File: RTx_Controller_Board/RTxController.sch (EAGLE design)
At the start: 204 parts, among them IC1 LTC4263, IC2 TLK110", SW1 COM08720, U1 STM32F407ZXT, U2 TPD4S012, X4 MINI-USB-32005-301

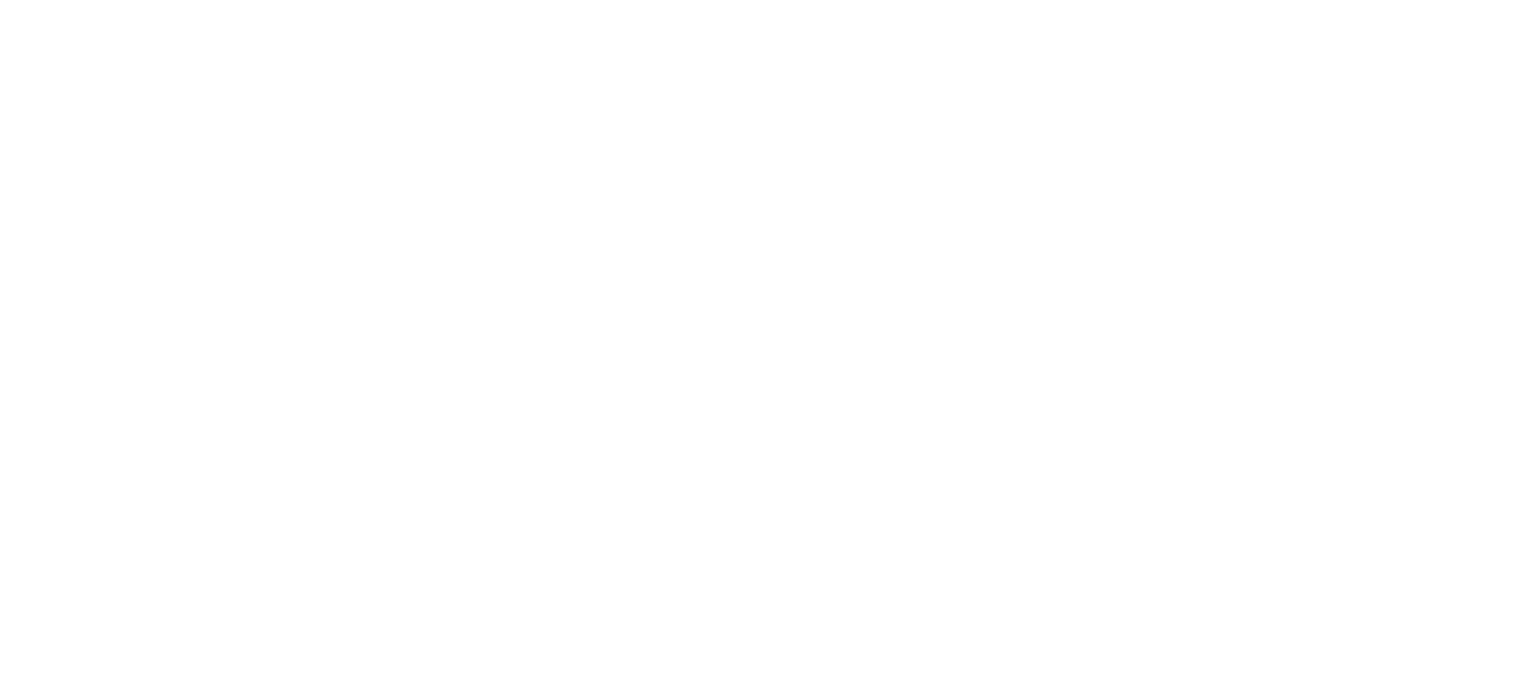
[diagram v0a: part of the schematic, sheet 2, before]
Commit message: Added PoE power supply to controller board.
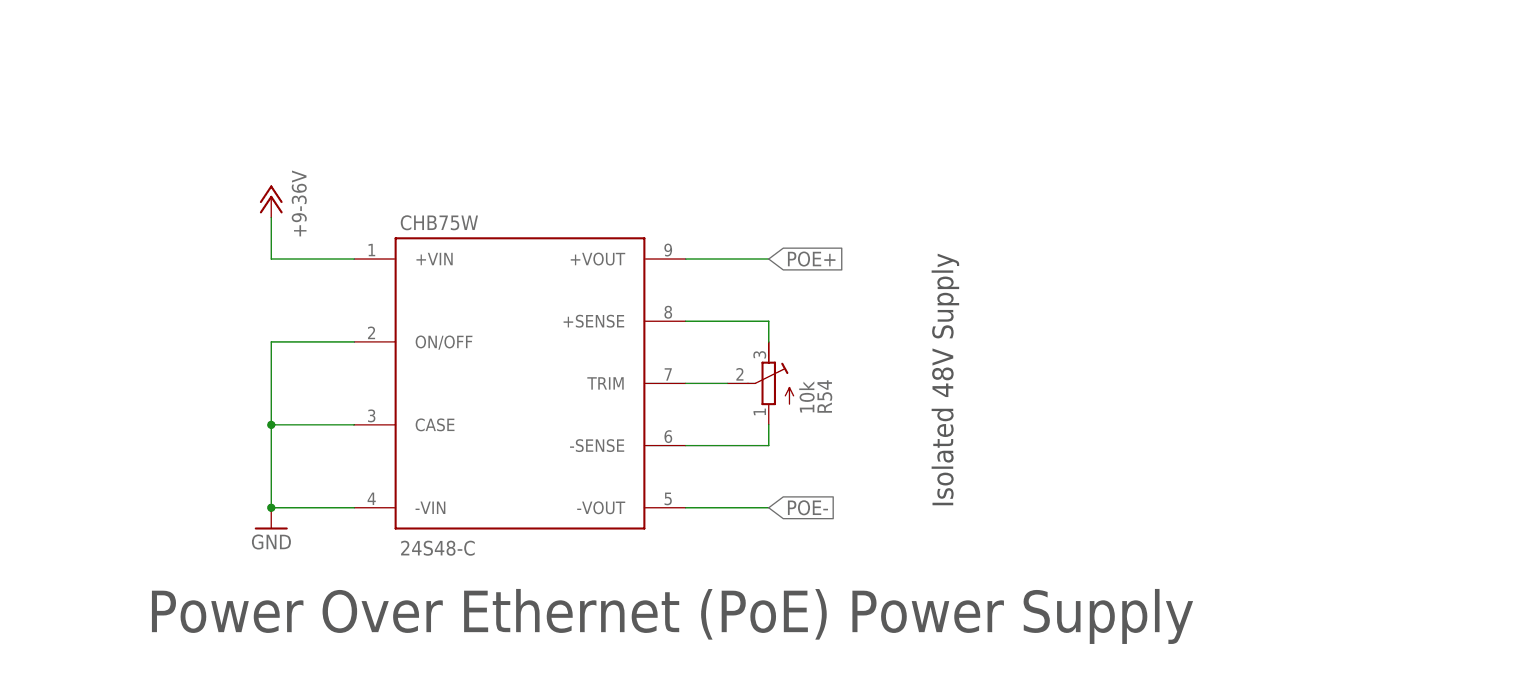
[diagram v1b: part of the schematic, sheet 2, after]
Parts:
- added 24S48-C: CHB75W, motorFeedback:CHB75W
- added R54: 10k, rcl:R-TRIMM4G/J
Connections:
- removed net DC+: C43.1, D1.C, D2.C, F1.1, IC1.VDD48, LED1.A
- removed net DC-: C43.2, C49.2, IC1.LEGACY, IC1.MIDSPAN, IC1.OSC, IC1.PWRMGT, IC1.VSS, IC1.VSS@1
- new net N$65: 24S48-C.TRIM@7, R54.S
- new net N$66: 24S48-C.-SENSE@6, R54.A
- new net N$67: 24S48-C.+SENSE@8, R54.E
- new net POE+: 24S48-C.+VOUT@9, C43.1, D1.C, D2.C, F1.1, IC1.VDD48, LED1.A
- new net POE-: 24S48-C.-VOUT@5, C43.2, C49.2, IC1.LEGACY, IC1.MIDSPAN, IC1.OSC, IC1.PWRMGT, IC1.VSS, IC1.VSS@1
- net +9-36V: now also 24S48-C.+VIN@1
- net GND: now also 24S48-C.-VIN@4, 24S48-C.CASE@3, 24S48-C.ON/OFF@2
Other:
- note added: "Power Over Ethernet (PoE) Power Supply"
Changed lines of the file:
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@@
 <part name="R52" library="motorFeedback" deviceset="R-US_" device="R0603"/>
 <part name="R53" library="motorFeedback" deviceset="R-US_" device="R0603"/>
+<part name="24S48-C" library="motorFeedback" deviceset="CHB75W" device=""/>
+<part name="R54" library="rcl" deviceset="R-TRIMM" device="4G/J" value="10k"/>
+<part name="GND97" library="motorFeedback" deviceset="GND" device=""/>
+<part name="U$7" library="motorFeedback" deviceset="+9-36V" device=""/>
 </parts>
 <sheets>
@@
 <text x="208.28" y="132.08" size="5.08" layer="97">Main Switching Power Supply</text>
 <text x="48.26" y="50.8" size="5.08" layer="97">Analog Reference Voltage Regulator</text>
+<text x="208.28" y="48.26" size="5.08" layer="97">Power Over Ethernet (PoE) Power Supply</text>
+<text x="307.086" y="63.5" size="2.54" layer="97" rot="R90">Isolated 48V Supply</text>
 </plain>
 <instances>
@@
 <instance part="REF2" gate="G$1" x="91.44" y="83.82"/>
 <instance part="P+24" gate="1" x="55.88" y="104.14"/>
+<instance part="24S48-C" gate="G$1" x="254" y="78.74" rot="MR180"/>
+<instance part="R54" gate="G$1" x="284.48" y="78.74" rot="MR0"/>
+<instance part="GND97" gate="1" x="223.52" y="60.96" rot="MR0"/>
+<instance part="U$7" gate="G$1" x="223.52" y="101.6" rot="MR0"/>
 </instances>
 <busses>
@@
 <pinref part="C24" gate="G$1" pin="2"/>
 <pinref part="GND24" gate="1" pin="GND"/>
+</segment>
+<segment>
+<pinref part="24S48-C" gate="G$1" pin="-VIN@4"/>
+<wire x1="233.68" y1="63.5" x2="223.52" y2="63.5" width="0.1524" layer="91"/>
+<pinref part="GND97" gate="1" pin="GND"/>
+<pinref part="24S48-C" gate="G$1" pin="CASE@3"/>
+<wire x1="233.68" y1="73.66" x2="223.52" y2="73.66" width="0.1524" layer="91"/>
+<wire x1="223.52" y1="73.66" x2="223.52" y2="63.5" width="0.1524" layer="91"/>
+<junction x="223.52" y="63.5"/>
+<pinref part="24S48-C" gate="G$1" pin="ON/OFF@2"/>
+<wire x1="233.68" y1="83.82" x2="223.52" y2="83.82" width="0.1524" layer="91"/>
+<wire x1="223.52" y1="83.82" x2="223.52" y2="73.66" width="0.1524" layer="91"/>
+<junction x="223.52" y="73.66"/>
 </segment>
 </net>
@@
 <pinref part="C34" gate="G$1" pin="+"/>
 </segment>
+<segment>
+<pinref part="24S48-C" gate="G$1" pin="+VIN@1"/>
+<wire x1="233.68" y1="93.98" x2="223.52" y2="93.98" width="0.1524" layer="91"/>
+<pinref part="U$7" gate="G$1" pin="+9-36V"/>
+<wire x1="223.52" y1="99.06" x2="223.52" y2="93.98" width="0.1524" layer="91"/>
+</segment>
 </net>
 <net name="+12V" class="0">
@@
 <pinref part="REF2" gate="G$1" pin="VIN@2"/>
 <pinref part="P+24" gate="1" pin="+18V"/>
+</segment>
+</net>
+<net name="N$65" class="0">
+<segment>
+<pinref part="R54" gate="G$1" pin="S"/>
+<pinref part="24S48-C" gate="G$1" pin="TRIM@7"/>
+<wire x1="279.4" y1="78.74" x2="274.32" y2="78.74" width="0.1524" layer="91"/>
+</segment>
+</net>
+<net name="N$66" class="0">
+<segment>
+<pinref part="R54" gate="G$1" pin="A"/>
+<pinref part="24S48-C" gate="G$1" pin="-SENSE@6"/>
+<wire x1="284.48" y1="73.66" x2="284.48" y2="71.12" width="0.1524" layer="91"/>
+<wire x1="284.48" y1="71.12" x2="274.32" y2="71.12" width="0.1524" layer="91"/>
+</segment>
+</net>
+<net name="N$67" class="0">
+<segment>
+<pinref part="R54" gate="G$1" pin="E"/>
+<pinref part="24S48-C" gate="G$1" pin="+SENSE@8"/>
+<wire x1="284.48" y1="83.82" x2="284.48" y2="86.36" width="0.1524" layer="91"/>
+<wire x1="284.48" y1="86.36" x2="274.32" y2="86.36" width="0.1524" layer="91"/>
+</segment>
+</net>
+<net name="POE-" class="0">
+<segment>
+<pinref part="24S48-C" gate="G$1" pin="-VOUT@5"/>
+<wire x1="274.32" y1="63.5" x2="284.48" y2="63.5" width="0.1524" layer="91"/>
+<label x="284.48" y="63.5" size="1.778" layer="95" rot="MR180" xref="yes"/>
+</segment>
+</net>
+<net name="POE+" class="0">
+<segment>
+<pinref part="24S48-C" gate="G$1" pin="+VOUT@9"/>
+<wire x1="274.32" y1="93.98" x2="284.48" y2="93.98" width="0.1524" layer="91"/>
+<label x="284.48" y="93.98" size="1.778" layer="95" rot="MR180" xref="yes"/>
 </segment>
 </net>
@@
 </segment>
 </net>
-<net name="DC-" class="0">
+<net name="POE-" class="0">
 <segment>
 <pinref part="IC1" gate="G$1" pin="LEGACY"/>
@@
 </segment>
 </net>
-<net name="DC+" class="0">
+<net name="POE+" class="0">
 <segment>
 <pinref part="D1" gate="G$1" pin="C"/>

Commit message: Added 8V power supply. Updated Ethernet documentation.
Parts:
- added C125: (no value), motorFeedback:CPOL-USB
- added C126: 0.1u, motorFeedback:C-EUC0402
- added VR3: TL751M08QKVURQ1, motorFeedback:TL751M08QKVURQ1
- renumbered 24S48-C to POE, U$6 to X8
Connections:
- removed net +18V: C24.1, C25.1, REF2.VIN@2
- new net +8V: C24.1, C25.1, REF2.VIN@2, VR3.OUT@4
- net +12V: now also C125.+, C126.1, VR3.I@2
- net GND: now also C125.-, C126.2, VR3.!EN!@1, VR3.GND@3
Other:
- note added: "Analog Power Supply"
- moved on the sheet: C26, C27, C28, C29, C30, C31, C32, C33, C34, C35, R11, R12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

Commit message: Added SWD connector, values for output pin ESD protection components.
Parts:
- added JP2: (no value), pinhead:PINHD-1X6
- added R55, R56, R57, R58: 22, motorFeedback:R-US_R0603
- added R59: 10k, motorFeedback:R-US_R0603
- C100, C105, C106, C107, C108, C113, C114, C115, C116, C121, C122, C123, C124, C97, C98, C99: value (none) -> NU
- C101, C102, C103, C104, C109, C110, C111, C112, C117, C118, C119, C120, C93, C94, C95, C96: value (none) -> 0.1u
- R37, R39, R40, R41, R42, R43, R44, R45, R46, R47, R48, R49, R50, R51, R52, R53: value (none) -> 200
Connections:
- net N$44 renamed BOOT0
- net VCAP_1@49 renamed VCAP_1
- net VCAP_2@73 renamed VCAP_2
- net VDDA@22 renamed VDDA
- removed net N$39: C92.1, SW1.1@1, SW1.3@3, U1-PWR.NRST@14
- new net NRST: C92.1, R55.1, SW1.1@1, SW1.3@3, U1-PWR.NRST@14
- new net STM_SWCLK: R57.1, U1-IO.PA14/JTCK@76
- new net STM_SWDIO: R56.1, U1-IO.PA13/JTMS@72
- new net STM_SWO: R58.1, U1-IO.PB3/JTDO@89
- new net SWD_GND1: JP2.1, R59.2
- new net SWD_NRST: JP2.5, R55.2
- new net SWD_SWCLK: JP2.2, R57.2
- new net SWD_SWDIO: JP2.4, R56.2
- new net SWD_SWO: JP2.6, R58.2
- net ENABLE_AXIS3_OUT: now also R41.2; no longer R46.2
- net ENABLE_AXIS4_OUT: now also R43.2; no longer R48.2
- net ENABLE_LAT_OUT: now also R51.2; no longer R43.2
- net ENABLE_VERT_OUT: now also R53.2; no longer R45.2
- net GND: now also JP2.3, R59.1
- net N$42: now also R45.1; no longer R37.1
- net N$45: now also R46.1; no longer R39.1
- net N$46: now also R47.1; no longer R40.1
- net N$47: now also R48.1; no longer R41.1
- net N$48: now also R49.1; no longer R42.1
- net N$49: now also R51.1; no longer R43.1
- net N$50: now also R52.1; no longer R44.1
- net N$51: now also R53.1; no longer R45.1
- net N$52: now also R41.1; no longer R46.1
- net N$53: now also R42.1; no longer R47.1
- net N$54: now also R43.1; no longer R48.1
- net N$55: now also R44.1; no longer R49.1
- net N$62: now also R37.1; no longer R51.1
- net N$63: now also R39.1; no longer R52.1
- net N$64: now also R40.1; no longer R53.1
- net PWM_AXIS3_U_OUT: now also R37.2; no longer R51.2
- net PWM_AXIS4_U_OUT: now also R40.2; no longer R53.2
- net PWM_AXIS4_V_OUT: now also R39.2; no longer R52.2
- net PWM_LAT_U_OUT: now also R48.2; no longer R41.2
- net PWM_LAT_V_OUT: now also R47.2; no longer R40.2
- net PWM_VERT_U_OUT: now also R46.2; no longer R39.2
- net PWM_VERT_V_OUT: now also R45.2; no longer R37.2
- net WATCHDOG_AXIS3_OUT: now also R42.2; no longer R47.2
- net WATCHDOG_AXIS4_OUT: now also R44.2; no longer R49.2
- net WATCHDOG_LAT_OUT: now also R49.2; no longer R42.2
- net WATCHDOG_VERT_OUT: now also R52.2; no longer R44.2
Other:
- note added: "SWD"
- moved on the sheet: C100, C101, C102, C103, C104, C105, C106, C107, C108, C93, C94, C95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

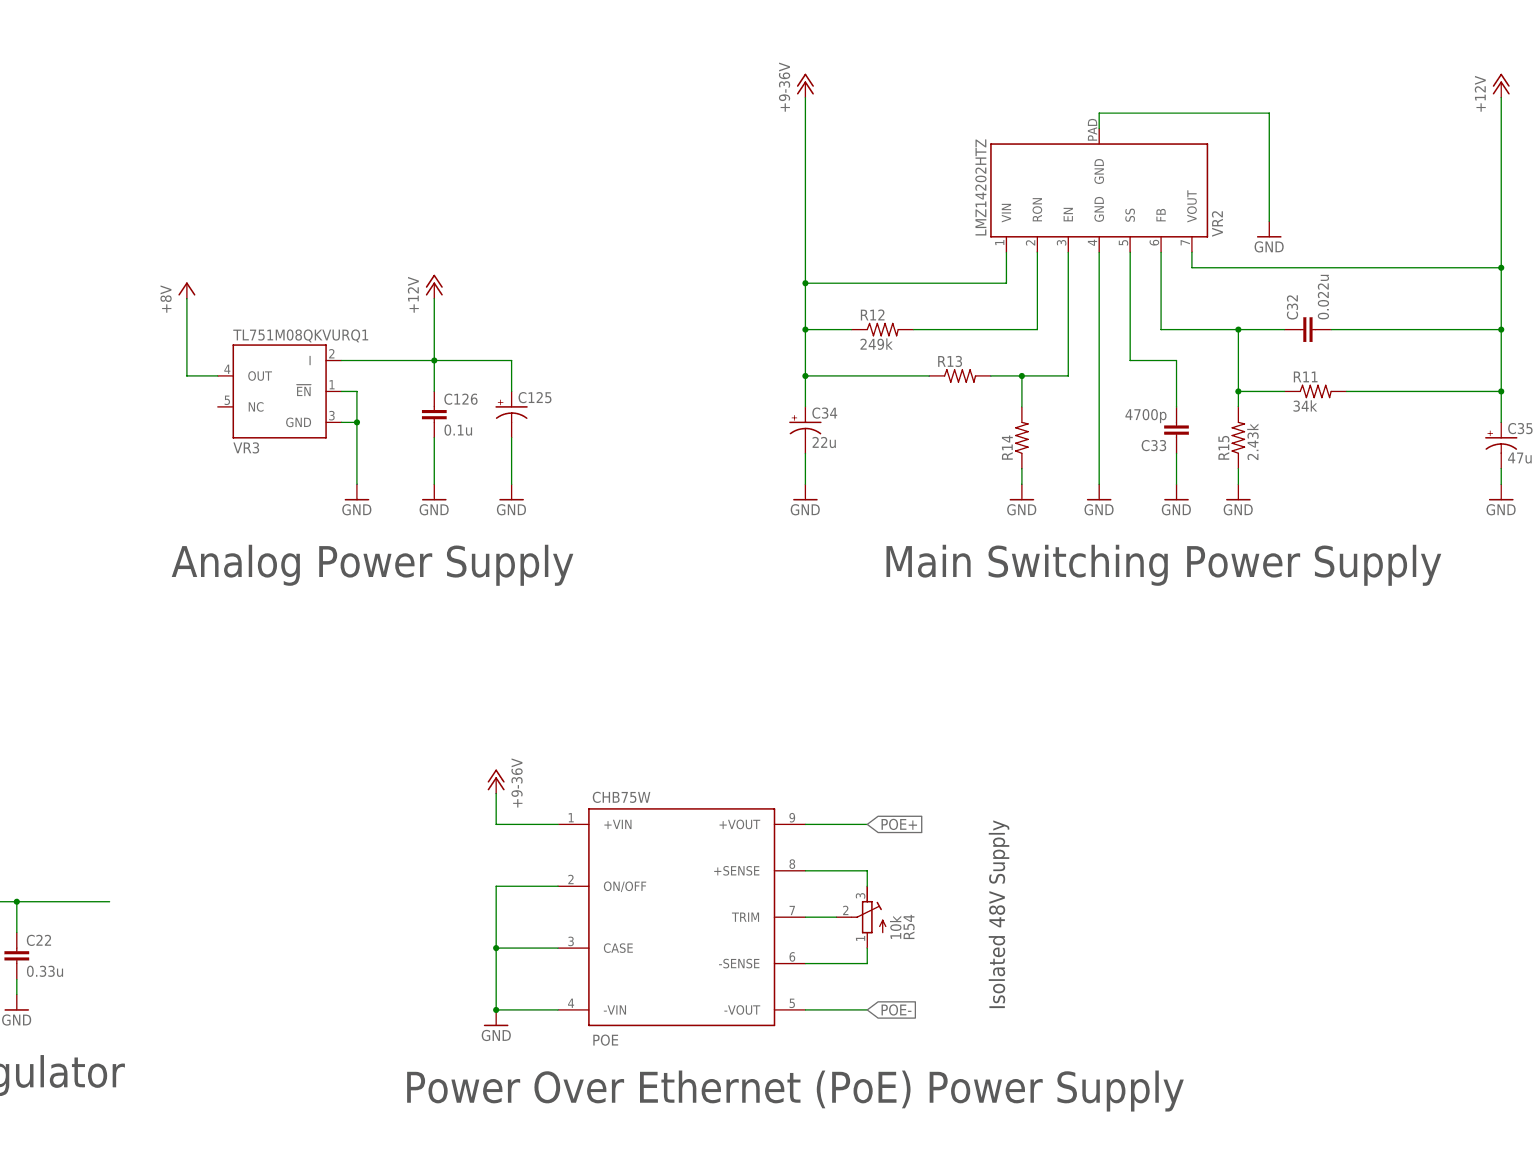
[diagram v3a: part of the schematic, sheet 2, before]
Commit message: Added capacitance to 8V and 48V PoE power supplies. Need to verify SPI daisy-chain pinout.
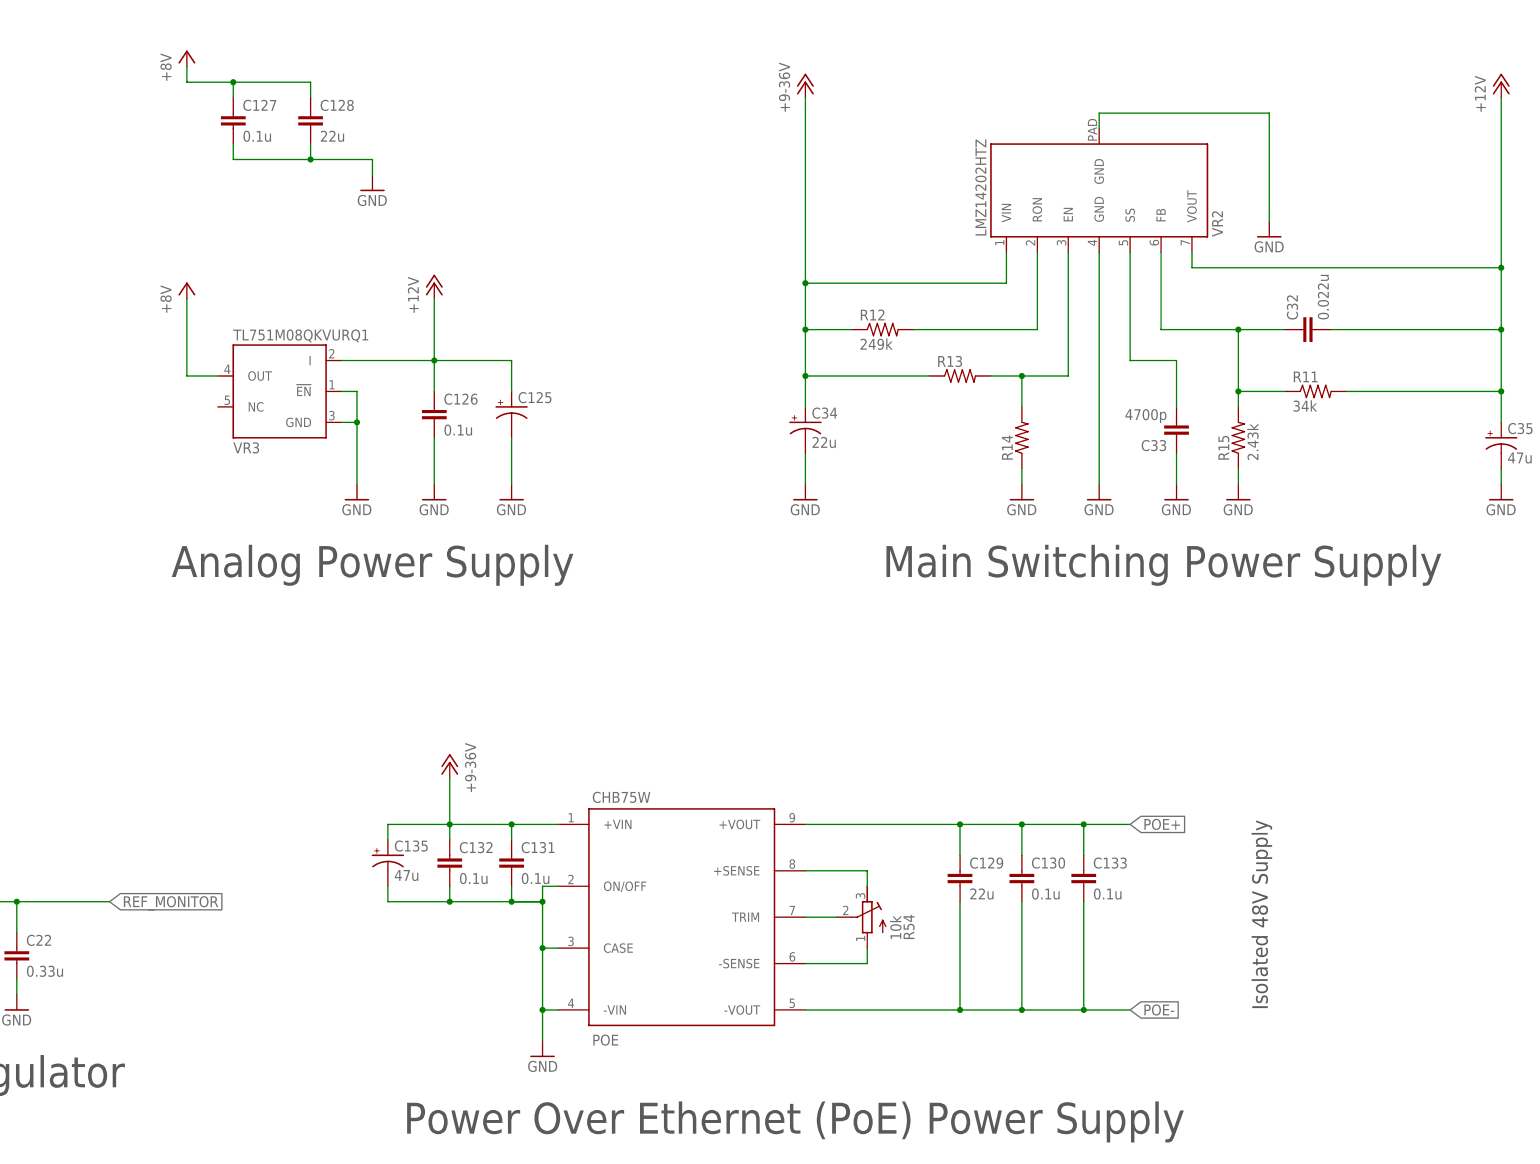
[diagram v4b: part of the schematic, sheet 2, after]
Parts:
- removed C54, C55, C72, C73, C74, C75, C76, C77: 0.1u, motorFeedback:C-EUC0402
- removed R16: 33, motorFeedback:R-US_R0402
- added C127, C130, C131, C132, C133: 0.1u, motorFeedback:C-EUC0402
- added C128, C129: 22u, motorFeedback:C-EUC1206
- added C135: 47u, motorFeedback:CPOL-USB
- JP1: value (none) -> NU
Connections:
- removed net N$21: C22.1, R10.2
- removed net SPI_NCS: U1-IO.PA4/SPI_NSS@29
- new net REF_MONITOR: C22.1, R10.2, U1-IO.PB2@37
- net +3.3V: no longer C54.1, C55.1, C72.1, C73.1, C74.1, C75.1, C76.1, C77.1
- net +5.000VREF: now also X1-9.F
- net +8V: now also C127.1, C128.1
- net +9-36V: now also C131.1, C132.1, C135.+
- net GND: now also C127.2, C128.2, C131.2, C132.2, C135.-, X1-2.F, X1-4.F, X1-6.F, X1-8.F; no longer C54.2, C55.2, C72.2, C73.2, C74.2, C75.2, C76.2, C77.2
- net N$14: now also X1-3.F
- net N$6: now also X1-7.F
- net N$7: now also X1-1.F
- net N$9: now also X1-5.F
- net POE+: now also C129.1, C130.1, C133.1
- net POE-: now also C129.2, C130.2, C133.2
- net SDO3: no longer R16.1
- net SPI_MISO: no longer R16.2
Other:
- note added: "JTAG access header"
- moved on the sheet: C78, C79, C80, C81, C82, C83, C84, C85, JP1, X1-1, X1-2, X1-3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
